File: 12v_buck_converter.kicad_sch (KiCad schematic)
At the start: 20 parts, among them IC1 TPS56A37RPAR, Q4 DMG4822SSD-13

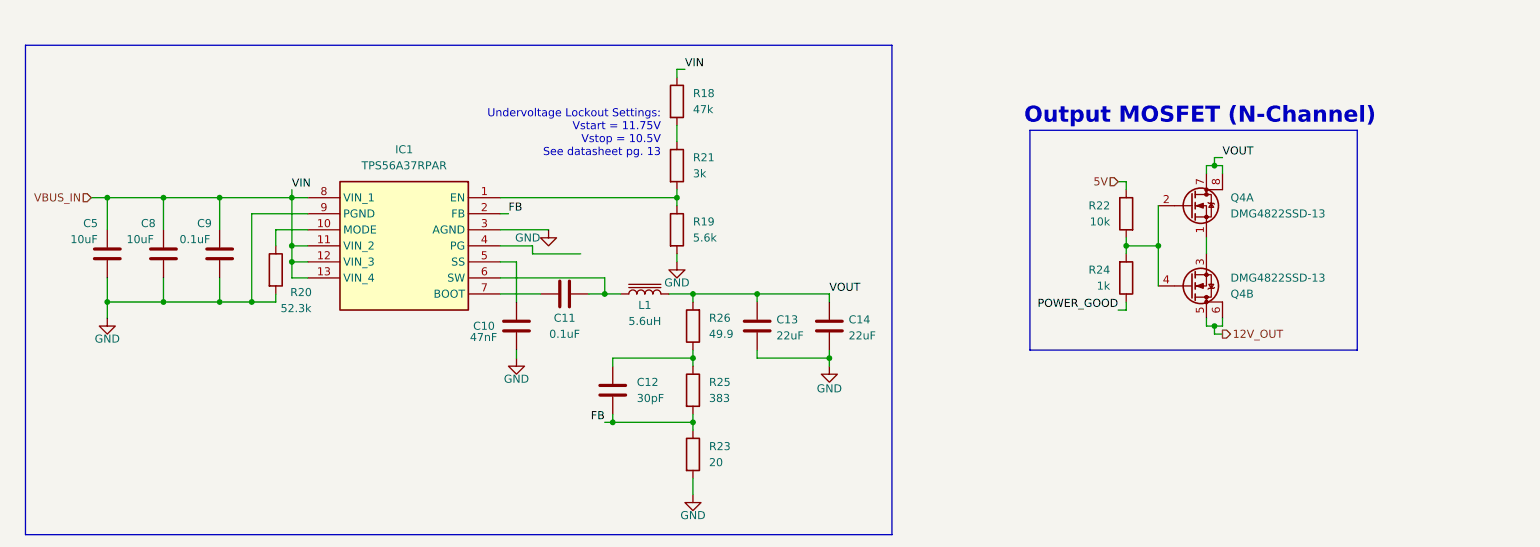
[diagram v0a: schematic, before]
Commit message: Finished 5V buck converter schematic
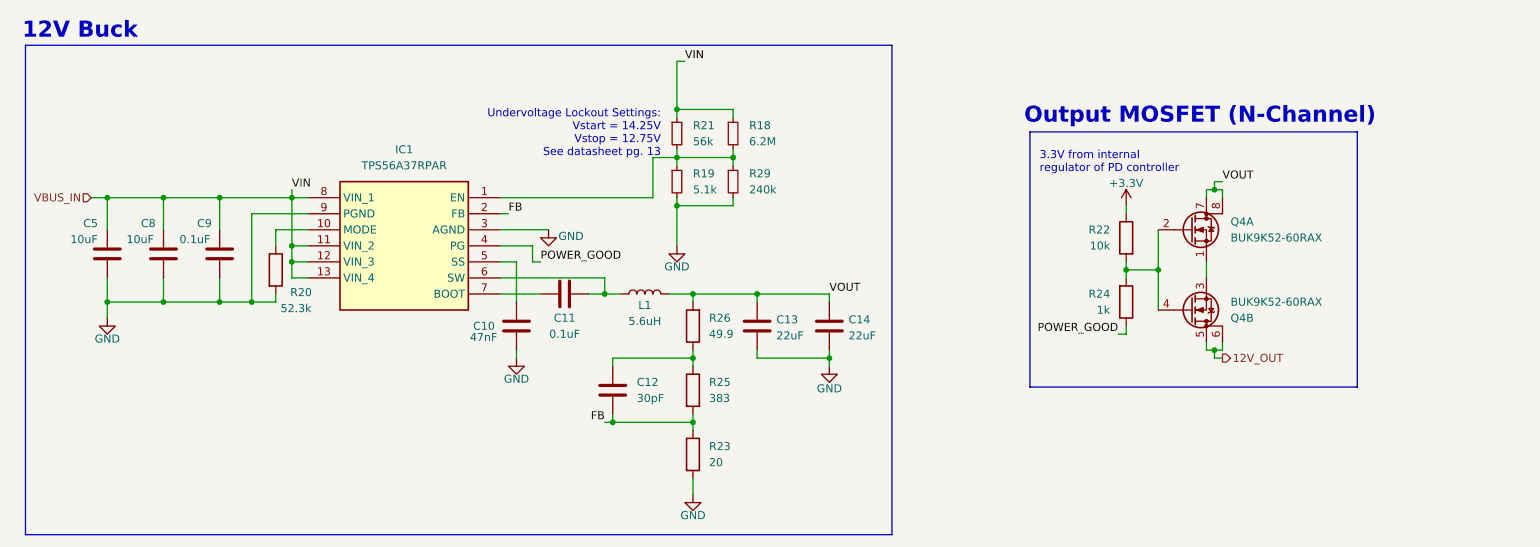
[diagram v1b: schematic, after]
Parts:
- added R29: 240k, symbol Device:R_Small
- L1: symbol Device:L_Iron -> Device:L
- Q4: value DMG4822SSD-13 -> BUK9K52-60RAX
- R18: value 47k -> 6.2M; symbol Device:R -> Device:R_Small
- R19: value 5.6k -> 5.1k; symbol Device:R -> Device:R_Small
- R21: value 3k -> 56k; symbol Device:R -> Device:R_Small
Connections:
- net GND: now also R29.2
- net POWER_GOOD: now also IC1.4 (PG)
- net VBUS_IN: now also R21.1
- net at R18.2: now also IC1.1 (EN), R19.1, R21.2, R29.1; no longer R21.1
- net 5V renamed +3.3V
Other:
- note added: "12V Buck"
- note added: "3.3V from internal regulator of PD controller"
- note added: "Undervoltage Lockout Settings: Vstart = 14.25V Vstop = 12.75V See datasheet pg. 13"
- note removed: "Undervoltage Lockout Settings: Vstart = 11.75V Vstop = 10.5V See datasheet pg. 13"
- company: (none) -> Longhorn Racing Solar
- moved on the sheet: Q4A, Q4B, R18, R19, R21, R22, R24

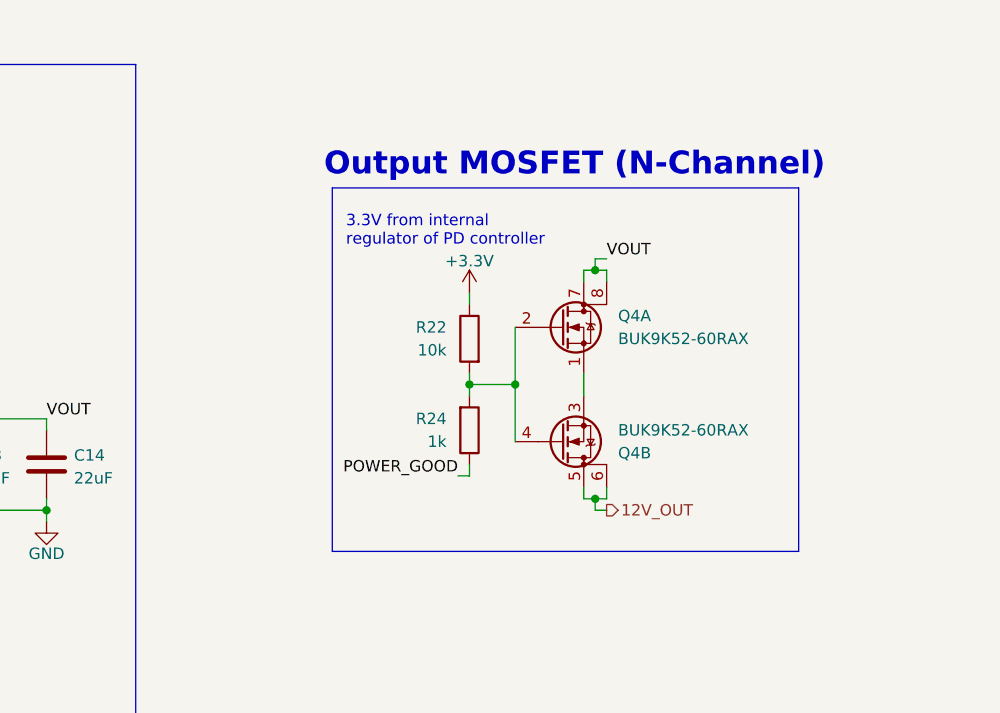
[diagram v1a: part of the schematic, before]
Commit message: added power good LED indicators
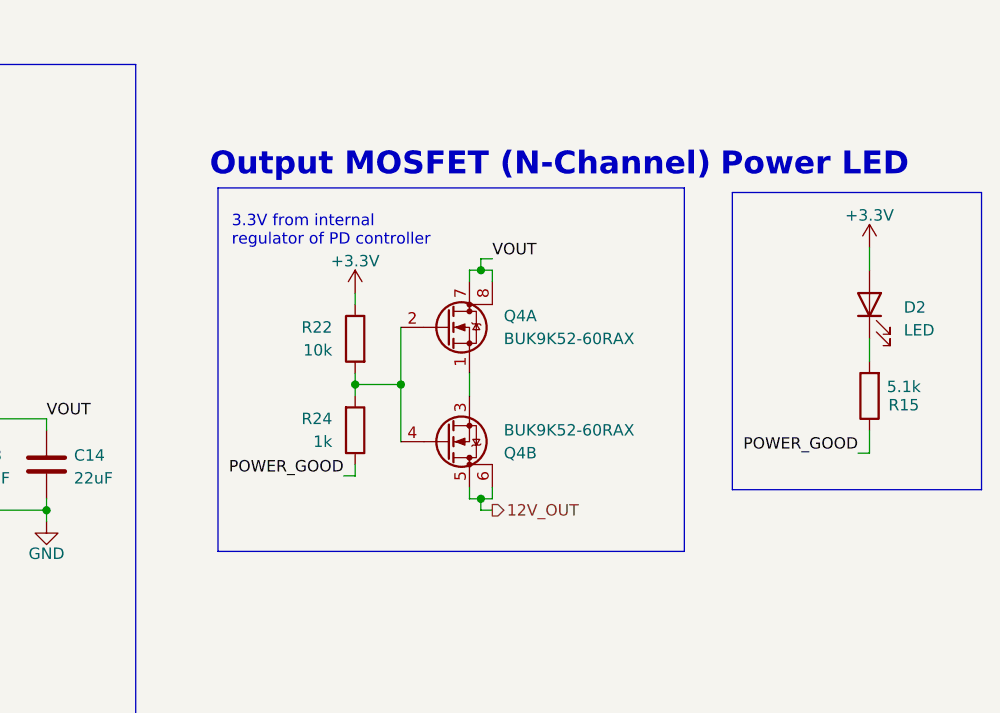
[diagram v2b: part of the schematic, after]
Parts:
- added D2: LED, symbol Device:LED
- added R15: 5.1k, symbol Device:R
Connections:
- net +3.3V: now also D2.2 (A)
- net POWER_GOOD: now also R15.1
- new net: D2.1 (K), R15.2
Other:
- note added: "Power LED"
- moved on the sheet: Q4A, Q4B, R22, R24

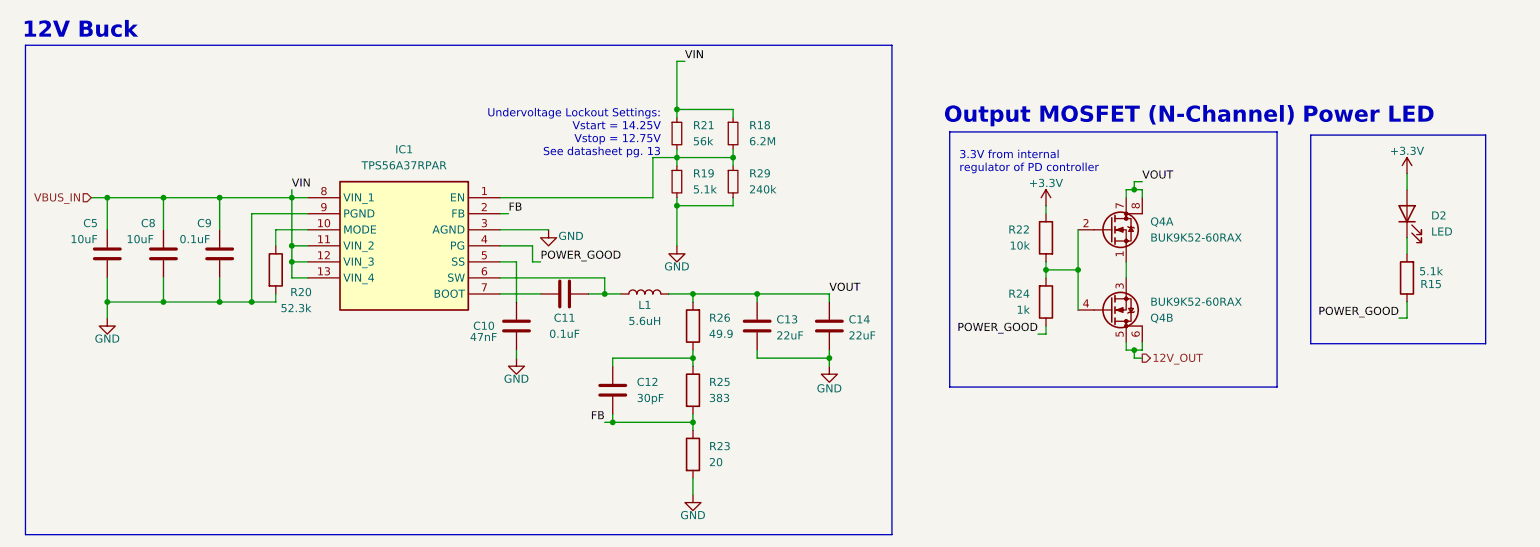
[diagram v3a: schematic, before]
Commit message: accidentally flipped current sense; also routed high level schematic
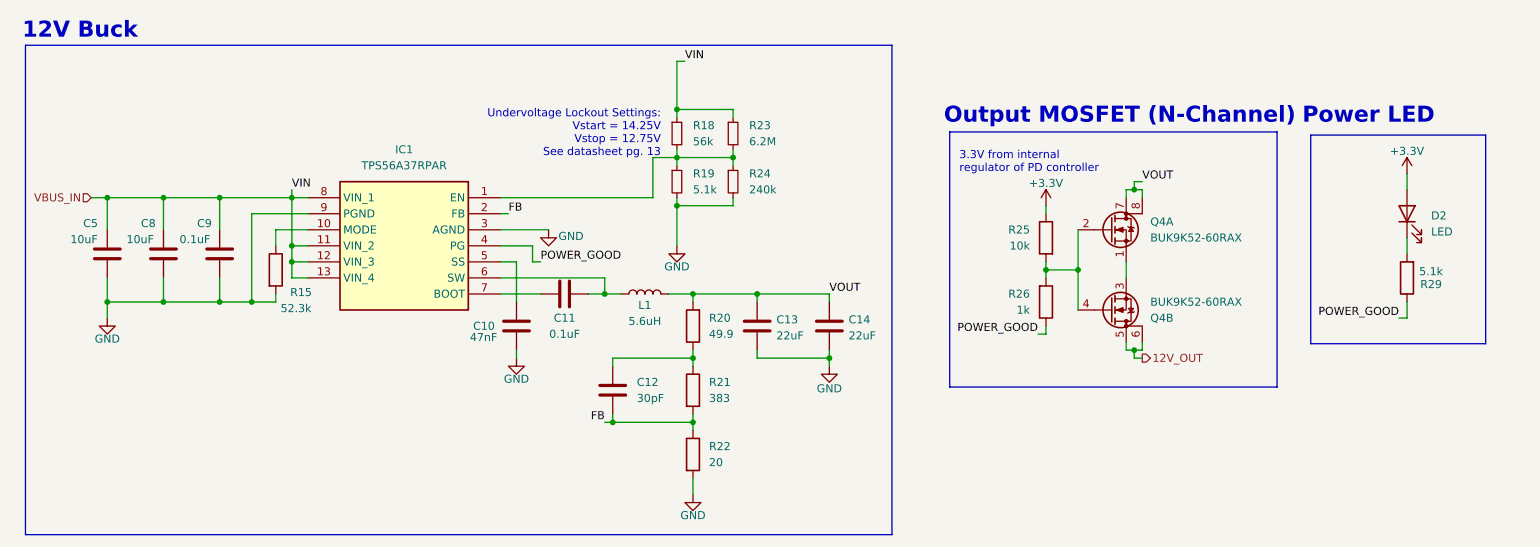
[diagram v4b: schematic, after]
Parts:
- renumbered R20 to R15, R21 to R18, R26 to R20, R25 to R21, R23 to R22, R18 to R23, R29 to R24, R22 to R25, R24 to R26, R15 to R29
